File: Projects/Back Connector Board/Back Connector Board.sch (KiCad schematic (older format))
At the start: 12 parts, among them J1 Conn_02x09_Odd_Even, J10 Molex_MiniFit_02x04, J11 Molex_MiniFit_02x04, J12 Molex_MiniFit_02x04, J2 Conn_02x09_Odd_Even, J3 Conn_02x09_Odd_Even, J4 Conn_02x09_Odd_Even, J5 Conn_02x08_Odd_Even, J6 Conn_02x08_Odd_Even, J7 Molex_MiniFit_02x04, J8 Molex_MiniFit_02x04, J9 Molex_MiniFit_02x04

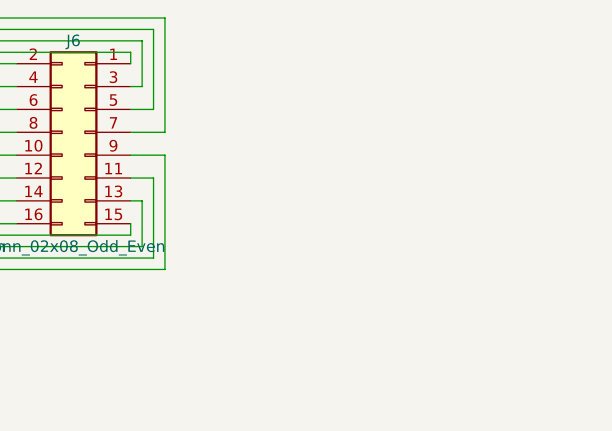
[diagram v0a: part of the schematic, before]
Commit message: Almost finished Back Connector Board; Just need to consult mechs
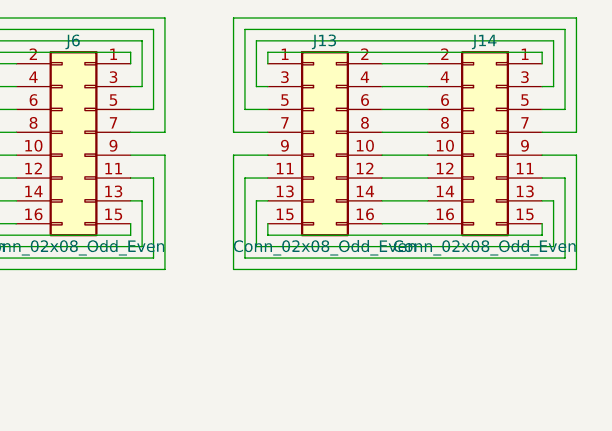
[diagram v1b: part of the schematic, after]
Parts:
- added J13, J14: Conn_02x08_Odd_Even, Pin_Headers:Pin_Header_Straight_2x08_Pitch2.54mm, symbol Conn_02x08_Odd_Even
- J5, J6: footprint Pin_Headers:Pin_Header_Angled_2x08_Pitch2.54mm -> Pin_Headers:Pin_Header_Straight_2x08_Pitch2.54mm
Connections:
- new net: J13.1 (Pin_1), J14.1 (Pin_1)
- new net: J13.10 (Pin_10), J14.10 (Pin_10)
- new net: J13.11 (Pin_11), J14.11 (Pin_11)
- new net: J13.12 (Pin_12), J14.12 (Pin_12)
- new net: J13.13 (Pin_13), J14.13 (Pin_13)
- new net: J13.14 (Pin_14), J14.14 (Pin_14)
- new net: J13.15 (Pin_15), J14.15 (Pin_15)
- new net: J13.16 (Pin_16), J14.16 (Pin_16)
- new net: J13.2 (Pin_2), J14.2 (Pin_2)
- new net: J13.3 (Pin_3), J14.3 (Pin_3)
- new net: J13.4 (Pin_4), J14.4 (Pin_4)
- new net: J13.5 (Pin_5), J14.5 (Pin_5)
- new net: J13.6 (Pin_6), J14.6 (Pin_6)
- new net: J13.7 (Pin_7), J14.7 (Pin_7)
- new net: J13.8 (Pin_8), J14.8 (Pin_8)
- new net: J13.9 (Pin_9), J14.9 (Pin_9)
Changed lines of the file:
@@
 F 0 "J5" H 6850 1750 50  0000 C CNN
 F 1 "Conn_02x08_Odd_Even" H 6850 850 50  0000 C CNN
-F 2 "Pin_Headers:Pin_Header_Angled_2x08_Pitch2.54mm" H 6800 1350 50  0001 C CNN
+F 2 "Pin_Headers:Pin_Header_Straight_2x08_Pitch2.54mm" H 6800 1350 50  0001 C CNN
 F 3 "" H 6800 1350 50  0001 C CNN
 	1    6800 1350
@@
 F 0 "J6" H 7650 1750 50  0000 C CNN
 F 1 "Conn_02x08_Odd_Even" H 7650 850 50  0000 C CNN
-F 2 "Pin_Headers:Pin_Header_Angled_2x08_Pitch2.54mm" H 7600 1350 50  0001 C CNN
+F 2 "Pin_Headers:Pin_Header_Straight_2x08_Pitch2.54mm" H 7600 1350 50  0001 C CNN
 F 3 "" H 7600 1350 50  0001 C CNN
 	1    7600 1350
@@
 Wire Wire Line
 	2200 4150 2200 4050
+$Comp
+L Conn_02x08_Odd_Even J13
+U 1 1 5ADC2CCE
+P 8600 1350
+F 0 "J13" H 8650 1750 50  0000 C CNN
+F 1 "Conn_02x08_Odd_Even" H 8650 850 50  0000 C CNN
+F 2 "Pin_Headers:Pin_Header_Straight_2x08_Pitch2.54mm" H 8600 1350 50  0001 C CNN
+F 3 "" H 8600 1350 50  0001 C CNN
+	1    8600 1350
+	1    0    0    -1
+$EndComp
+$Comp
+L Conn_02x08_Odd_Even J14
+U 1 1 5ADC2CD4
+P 9400 1350
+F 0 "J14" H 9450 1750 50  0000 C CNN
+F 1 "Conn_02x08_Odd_Even" H 9450 850 50  0000 C CNN
+F 2 "Pin_Headers:Pin_Header_Straight_2x08_Pitch2.54mm" H 9400 1350 50  0001 C CNN
+F 3 "" H 9400 1350 50  0001 C CNN
+	1    9400 1350
+	-1   0    0    -1
+$EndComp
+Wire Wire Line
+	8900 1050 9100 1050
+Wire Wire Line
+	8900 1150 9100 1150
+Wire Wire Line
+	8900 1250 9100 1250
+Wire Wire Line
+	8900 1350 9100 1350
+Wire Wire Line
+	8900 1450 9100 1450
+Wire Wire Line
+	8900 1550 9100 1550
+Wire Wire Line
+	8900 1650 9100 1650
+Wire Wire Line
+	8900 1750 9100 1750
+Wire Wire Line
+	9600 1750 9600 1800
+Wire Wire Line
+	9600 1800 8400 1800
+Wire Wire Line
+	8400 1800 8400 1750
+Wire Wire Line
+	8400 1650 8350 1650
+Wire Wire Line
+	8350 1650 8350 1850
+Wire Wire Line
+	8350 1850 9650 1850
+Wire Wire Line
+	9650 1850 9650 1650
+Wire Wire Line
+	9650 1650 9600 1650
+Wire Wire Line
+	9600 1550 9700 1550
+Wire Wire Line
+	9700 1550 9700 1900
+Wire Wire Line
+	9700 1900 8300 1900
+Wire Wire Line
+	8300 1900 8300 1550
+Wire Wire Line
+	8300 1550 8400 1550
+Wire Wire Line
+	8400 1450 8250 1450
+Wire Wire Line
+	8250 1450 8250 1950
+Wire Wire Line
+	8250 1950 9750 1950
+Wire Wire Line
+	9750 1950 9750 1450
+Wire Wire Line
+	9750 1450 9600 1450
+Wire Wire Line
+	9600 1050 9600 1000
+Wire Wire Line
+	9600 1000 8400 1000
+Wire Wire Line
+	8400 1000 8400 1050
+Wire Wire Line
+	8400 1150 8350 1150
+Wire Wire Line
+	8350 1150 8350 950
+Wire Wire Line
+	8350 950  9650 950
+Wire Wire Line
+	9650 950  9650 1150
+Wire Wire Line
+	9650 1150 9600 1150
+Wire Wire Line
+	9600 1250 9700 1250
+Wire Wire Line
+	9700 1250 9700 900
+Wire Wire Line
+	9700 900  8300 900
+Wire Wire Line
+	8300 900  8300 1250
+Wire Wire Line
+	8300 1250 8400 1250
+Wire Wire Line
+	8400 1350 8250 1350
+Wire Wire Line
+	8250 1350 8250 850
+Wire Wire Line
+	8250 850  9750 850
+Wire Wire Line
+	9750 850  9750 1350
+Wire Wire Line
+	9750 1350 9600 1350
 $EndSCHEMATC

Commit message: Finished Back connector board to account for RPi cams
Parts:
- J1, J2, J3, J4: footprint USST-footprints:USB-A_3.0_Stacked_WM10420-ND -> USST-footprints:USBA_3.0_Stacked_Vertical-Molex_48409
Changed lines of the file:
@@
 F 0 "J1" H 2400 1950 50  0000 C CNN
 F 1 "Conn_02x09_Odd_Even" H 2400 950 50  0000 C CNN
-F 2 "USST-footprints:USB-A_3.0_Stacked_WM10420-ND" H 2350 1450 50  0001 C CNN
+F 2 "USST-footprints:USBA_3.0_Stacked_Vertical-Molex_48409" H 2350 1450 50  0001 C CNN
 F 3 "" H 2350 1450 50  0001 C CNN
 	1    2350 1450
@@
 F 0 "J2" H 3325 1950 50  0000 C CNN
 F 1 "Conn_02x09_Odd_Even" H 3325 950 50  0000 C CNN
-F 2 "USST-footprints:USB-A_3.0_Stacked_WM10420-ND" H 3275 1450 50  0001 C CNN
+F 2 "USST-footprints:USBA_3.0_Stacked_Vertical-Molex_48409" H 3275 1450 50  0001 C CNN
 F 3 "" H 3275 1450 50  0001 C CNN
 	1    3275 1450
@@
 F 0 "J3" H 4475 1950 50  0000 C CNN
 F 1 "Conn_02x09_Odd_Even" H 4475 950 50  0000 C CNN
-F 2 "USST-footprints:USB-A_3.0_Stacked_WM10420-ND" H 4425 1450 50  0001 C CNN
+F 2 "USST-footprints:USBA_3.0_Stacked_Vertical-Molex_48409" H 4425 1450 50  0001 C CNN
 F 3 "" H 4425 1450 50  0001 C CNN
 	1    4425 1450
@@
 F 0 "J4" H 5400 1950 50  0000 C CNN
 F 1 "Conn_02x09_Odd_Even" H 5400 950 50  0000 C CNN
-F 2 "USST-footprints:USB-A_3.0_Stacked_WM10420-ND" H 5350 1450 50  0001 C CNN
+F 2 "USST-footprints:USBA_3.0_Stacked_Vertical-Molex_48409" H 5350 1450 50  0001 C CNN
 F 3 "" H 5350 1450 50  0001 C CNN
 	1    5350 1450
